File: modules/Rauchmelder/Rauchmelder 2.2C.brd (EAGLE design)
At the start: 38 x 65 mm, 49 parts, among them IC1 MC34063AD, IC3 LPC922FDH, Q1 BC856, Q3 BCP52, T1 BC848

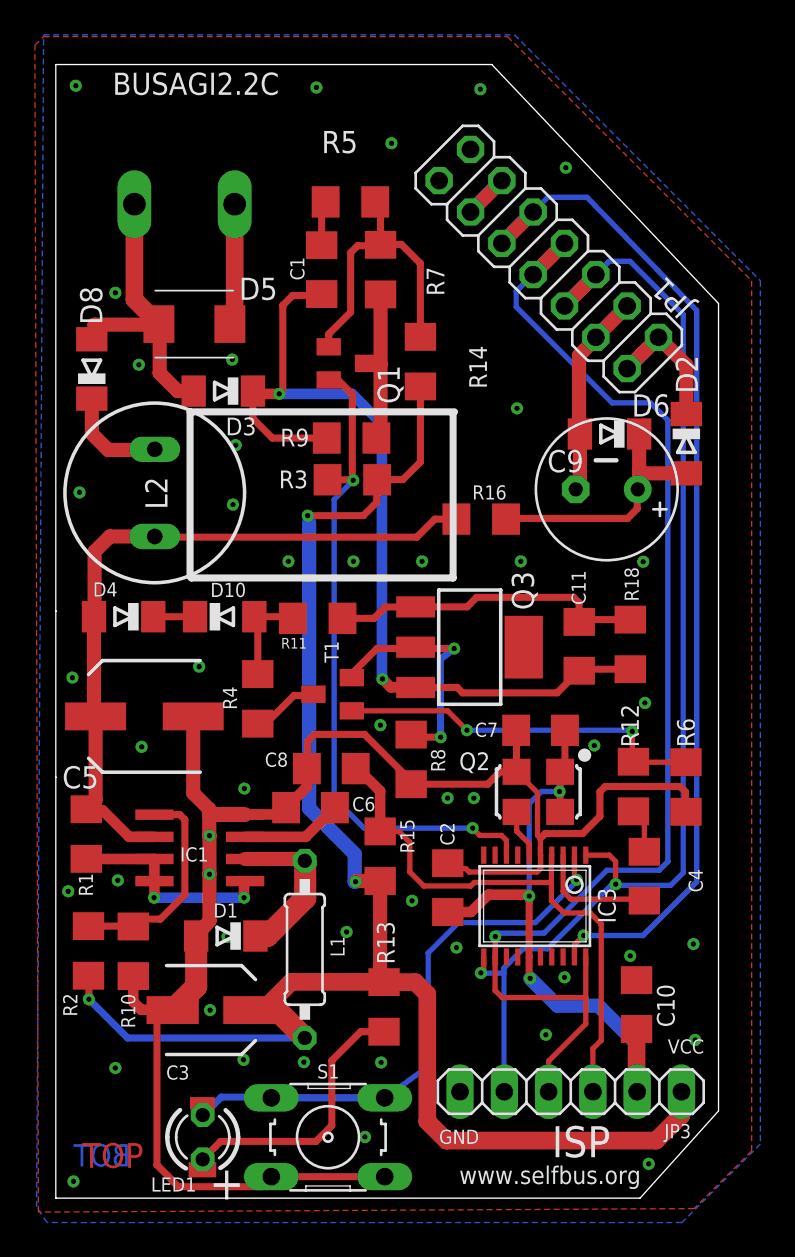
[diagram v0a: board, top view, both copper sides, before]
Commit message: RM2.2C, add some GND Vias
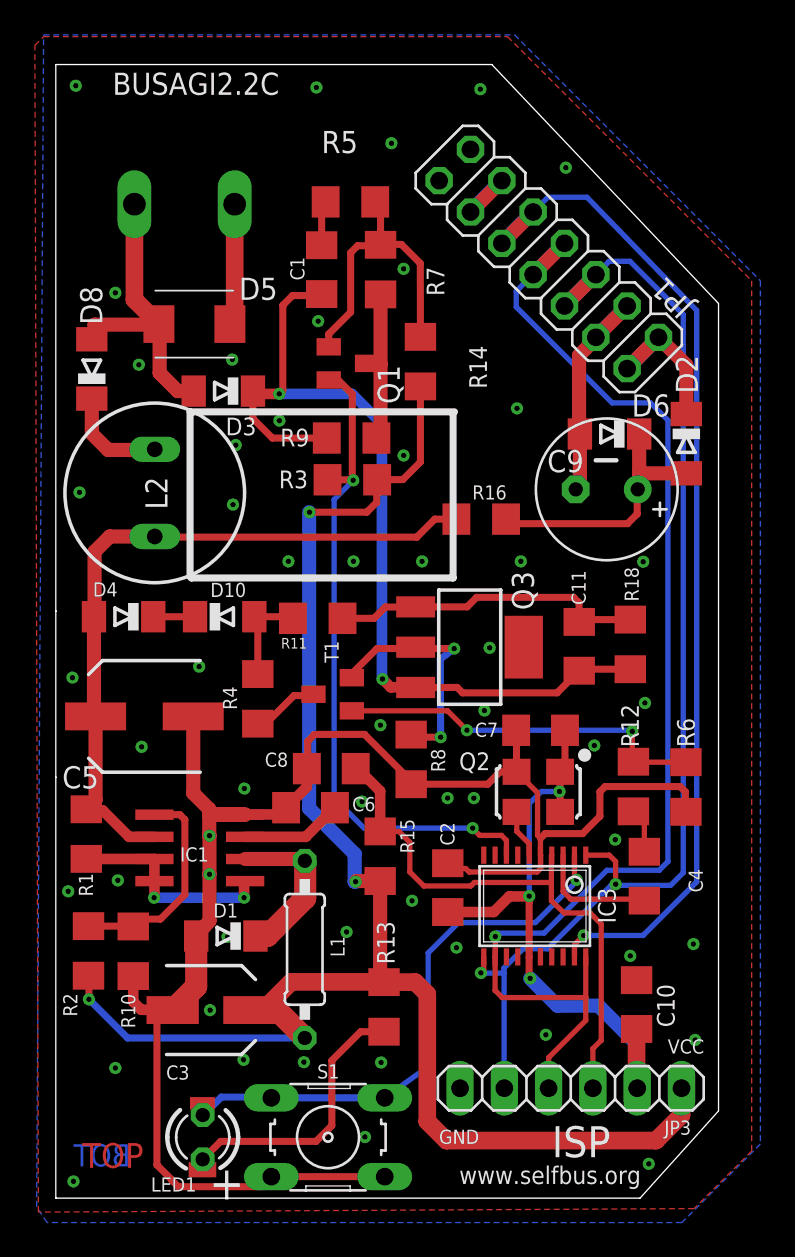
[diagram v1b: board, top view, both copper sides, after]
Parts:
- moved JP3 0.20 mm to (29.5, 6.30)
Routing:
- net N$10: track 14.8 -> 15.3 mm
- net GND: vias 47 -> 54
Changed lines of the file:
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@@
 <attribute name="VALUE" x="21.3783" y="16.297925" size="1.016" layer="27" ratio="10" rot="R90"/>
 </element>
-<element name="JP3" library="pinhead" package="1X06" value="" x="29.5274" y="6.1023" smashed="yes" rot="R180">
-<attribute name="NAME" x="36.4273" y="4.247925" size="0.8128" layer="25" ratio="10" rot="R180"/>
-<attribute name="VALUE" x="37.1474" y="9.2773" size="1.27" layer="27" rot="R180"/>
+<element name="JP3" library="pinhead" package="1X06" value="" x="29.5274" y="6.3023" smashed="yes" rot="R180">
+<attribute name="NAME" x="36.4273" y="4.447925" size="0.8128" layer="25" ratio="10" rot="R180"/>
+<attribute name="VALUE" x="37.1474" y="9.4773" size="1.27" layer="27" rot="R180"/>
 </element>
 <element name="C4" library="rcl" package="C1206" value="10n" x="33.74485" y="18.4599" smashed="yes" rot="R270">
@@
 <wire x1="36.1" y1="22.1" x2="36.433125" y2="22.152025" width="0.4064" layer="1"/>
 <wire x1="36.433125" y1="22.152025" x2="36.132975" y2="22.152175" width="0.4064" layer="1"/>
-<via x="29.171875" y="12.661875" extent="1-16" drill="0.3"/>
 <via x="28.09875" y="9.36625" extent="1-16" drill="0.3"/>
 <via x="10.31875" y="43.18" extent="1-16" drill="0.3"/>
@@
 <via x="1.013125" y="0.96125" extent="1-16" drill="0.3"/>
 <via x="33.99875" y="1.96625" extent="1-16" drill="0.3"/>
+<via x="19.943125" y="42.585625" extent="1-16" drill="0.3"/>
+<via x="15.043125" y="50.285625" extent="1-16" drill="0.3"/>
+<via x="12.81875" y="44.58" extent="1-16" drill="0.3"/>
+<via x="19.943125" y="53.285625" extent="1-16" drill="0.3"/>
+<via x="24.576875" y="27.955625" extent="1-16" drill="0.3"/>
+<via x="24.876875" y="31.555625" extent="1-16" drill="0.3"/>
+<via x="32.076875" y="20.555625" extent="1-16" drill="0.3"/>
+<via x="17.563125" y="22.739375" extent="1-16" drill="0.3"/>
 </signal>
 <signal name="VCC">
@@
 <via x="17.1925" y="18.141875" extent="1-16" drill="0.3"/>
 <wire x1="17.13375" y1="19.741875" x2="14.525625" y2="22.35" width="0.8128" layer="16"/>
-<wire x1="14.525625" y1="22.35" x2="14.525625" y2="38.735" width="0.8128" layer="16"/>
-<wire x1="14.525625" y1="38.735" x2="14.44625" y2="39.131875" width="0.4064" layer="16"/>
-<via x="14.44625" y="39.131875" extent="1-16" drill="0.3"/>
+<wire x1="14.525625" y1="22.35" x2="14.525625" y2="39.335" width="0.8128" layer="16"/>
+<wire x1="14.525625" y1="39.335" x2="14.54625" y2="39.331875" width="0.4064" layer="16"/>
+<via x="14.54625" y="39.331875" extent="1-16" drill="0.3"/>
 <wire x1="14.2774" y1="9.182975" x2="12.660375" y2="10.8" width="1.27" layer="1"/>
 <wire x1="12.660375" y1="10.8" x2="11.2" y2="10.8" width="1.27" layer="1"/>
@@
 <wire x1="22.4" y1="3.3" x2="34.415" y2="3.3" width="1.016" layer="1"/>
 <wire x1="34.415" y1="3.3" x2="35.8774" y2="4.7624" width="1.016" layer="1"/>
-<wire x1="35.8774" y1="4.7624" x2="35.8774" y2="6.1023" width="1.016" layer="1"/>
+<wire x1="35.8774" y1="4.7624" x2="35.8774" y2="6.3023" width="1.016" layer="1"/>
 <wire x1="20.90755" y1="46.542375" x2="20.90755" y2="42.20755" width="0.4064" layer="1"/>
 <wire x1="20.90755" y1="42.20755" x2="19.9" y2="41.2" width="0.4064" layer="1"/>
 <wire x1="19.9" y1="41.2" x2="18.42575" y2="41.189925" width="0.4064" layer="1"/>
-<wire x1="14.44625" y1="39.131875" x2="17.631875" y2="39.131875" width="0.4064" layer="1"/>
-<wire x1="17.631875" y1="39.131875" x2="18.4" y2="39.9" width="0.4064" layer="1"/>
+<wire x1="14.54625" y1="39.331875" x2="17.831875" y2="39.331875" width="0.4064" layer="1"/>
+<wire x1="17.831875" y1="39.331875" x2="18.4" y2="39.9" width="0.4064" layer="1"/>
 <wire x1="18.4" y1="39.9" x2="18.4" y2="41.164175" width="0.4064" layer="1"/>
 <wire x1="18.4" y1="41.164175" x2="18.42575" y2="41.189925" width="0.4064" layer="1"/>
@@
 <wire x1="33.483125" y1="41.559375" x2="33.45" y2="41.5925" width="0.4064" layer="1"/>
 <wire x1="25.814" y1="38.9337" x2="25.820675" y2="38.9337" width="0.4064" layer="1"/>
-<wire x1="25.820675" y1="38.9337" x2="25.98125" y2="38.973125" width="0.4064" layer="1"/>
-<wire x1="25.98125" y1="38.973125" x2="32.781875" y2="38.973125" width="0.4064" layer="1"/>
-<wire x1="32.781875" y1="38.973125" x2="33.3375" y2="39.52875" width="0.4064" layer="1"/>
-<wire x1="33.3375" y1="39.52875" x2="33.3375" y2="40.6083" width="0.4064" layer="1"/>
+<wire x1="25.820675" y1="38.9337" x2="25.88125" y2="38.673125" width="0.4064" layer="1"/>
+<wire x1="25.88125" y1="38.673125" x2="32.781875" y2="38.673125" width="0.4064" layer="1"/>
+<wire x1="32.781875" y1="38.673125" x2="33.3375" y2="39.22875" width="0.4064" layer="1"/>
+<wire x1="33.3375" y1="39.22875" x2="33.3375" y2="40.6083" width="0.4064" layer="1"/>
 <wire x1="33.3375" y1="40.6083" x2="33.369225" y2="40.640025" width="0.4064" layer="1"/>
 </signal>
@@
 <wire x1="26.8" y1="14.3" x2="25.7" y2="13.2" width="0.3048" layer="16"/>
 <wire x1="25.7" y1="12.9" x2="25.7" y2="6.1197" width="0.3048" layer="16"/>
-<wire x1="25.7" y1="6.1197" x2="25.7174" y2="6.1023" width="0.3048" layer="16"/>
+<wire x1="25.7" y1="6.1197" x2="25.7174" y2="6.3023" width="0.3048" layer="16"/>
 <wire x1="25.7" y1="13.2" x2="25.7" y2="12.9" width="0.3048" layer="16"/>
 <wire x1="25.7" y1="12.9" x2="24.385625" y2="12.9" width="0.3048" layer="16"/>
@@
 <contactref element="IC3" pad="12"/>
 <wire x1="30.38875" y1="13.830325" x2="30.38875" y2="11.5" width="0.3048" layer="1"/>
-<wire x1="30.38875" y1="11.5" x2="30.38875" y2="9.989375" width="0.3048" layer="1"/>
-<wire x1="30.38875" y1="9.989375" x2="28.2575" y2="7.858125" width="0.3048" layer="1"/>
-<wire x1="28.2575" y1="7.858125" x2="28.2575" y2="6.1024" width="0.3048" layer="1"/>
-<wire x1="28.2575" y1="6.1024" x2="28.2574" y2="6.1023" width="0.3048" layer="1"/>
+<wire x1="30.38875" y1="11.5" x2="30.38875" y2="10.189375" width="0.3048" layer="1"/>
+<wire x1="30.38875" y1="10.189375" x2="28.2575" y2="8.058125" width="0.3048" layer="1"/>
+<wire x1="28.2575" y1="8.058125" x2="28.2575" y2="6.1024" width="0.3048" layer="1"/>
+<wire x1="28.2575" y1="6.1024" x2="28.2574" y2="6.3023" width="0.3048" layer="1"/>
 <wire x1="29.168025" y1="54.748025" x2="27.371971875" y2="52.951971875" width="0.8128" layer="1"/>
 <wire x1="27.371971875" y1="52.951971875" x2="27.351971875" y2="52.951971875" width="0.4064" layer="16"/>
@@
 <wire x1="31.115" y1="11.033125" x2="33.3375" y2="8.810625" width="0.8128" layer="16"/>
 <wire x1="33.3375" y1="8.810625" x2="33.3375" y2="6.1024" width="0.8128" layer="16"/>
-<wire x1="33.3375" y1="6.1024" x2="33.3374" y2="6.1023" width="0.6096" layer="16"/>
-<wire x1="22.475" y1="16.405525" x2="23.805525" y2="16.405525" width="0.6096" layer="1"/>
-<wire x1="23.805525" y1="16.405525" x2="24.8" y2="17.4" width="0.6096" layer="1"/>
-<wire x1="24.8" y1="17.4" x2="27.0675" y2="17.4" width="0.6096" layer="1"/>
-<wire x1="27.0675" y1="17.4" x2="27.14625" y2="17.32125" width="0.6096" layer="1"/>
+<wire x1="33.3375" y1="6.1024" x2="33.3374" y2="6.3023" width="0.6096" layer="16"/>
+<wire x1="22.475" y1="16.405525" x2="25.105525" y2="16.405525" width="0.6096" layer="1"/>
+<wire x1="25.105525" y1="16.405525" x2="26" y2="17.3" width="0.6096" layer="1"/>
+<wire x1="26" y1="17.3" x2="27.1675" y2="17.3" width="0.6096" layer="1"/>
+<wire x1="27.1675" y1="17.3" x2="27.14625" y2="17.32125" width="0.6096" layer="1"/>
 <wire x1="27.13875" y1="13.830325" x2="27.13875" y2="12.66125" width="0.4064" layer="1"/>
 <wire x1="27.13875" y1="12.66125" x2="27.2" y2="12.6" width="0.4064" layer="1"/>
@@
 <contactref element="C10" pad="2"/>
 <wire x1="33.3" y1="9.7" x2="33.3" y2="6.1397" width="1.016" layer="1"/>
-<wire x1="33.3" y1="6.1397" x2="33.3374" y2="6.1023" width="1.016" layer="1"/>
+<wire x1="33.3" y1="6.1397" x2="33.3374" y2="6.3023" width="1.016" layer="1"/>
 </signal>
 <signal name="N$19">
@@
 <wire x1="17.145" y1="24.79385" x2="17.195525" y2="24.626875" width="0.4064" layer="1"/>
 <wire x1="28.41625" y1="19.643425" x2="28.43875" y2="19.665925" width="0.3048" layer="1"/>
-<wire x1="30.7974" y1="6.1023" x2="30.7974" y2="8.5724" width="0.3048" layer="1"/>
+<wire x1="30.7974" y1="6.3023" x2="30.7974" y2="8.5724" width="0.3048" layer="1"/>
 <wire x1="30.7974" y1="8.5724" x2="31.27375" y2="9.04875" width="0.3048" layer="1"/>
 <wire x1="31.27375" y1="9.04875" x2="31.27375" y2="15.71625" width="0.3048" layer="1"/>
